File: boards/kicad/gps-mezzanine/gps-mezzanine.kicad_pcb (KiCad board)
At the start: 2 copper layers, 55 x 40 mm, 15 parts, among them P1 CONN_02X20, Q1 BSS138, Q2 BSS138, U1 MCP1700T-3302E/TT, U2 FGPMMOPA6H

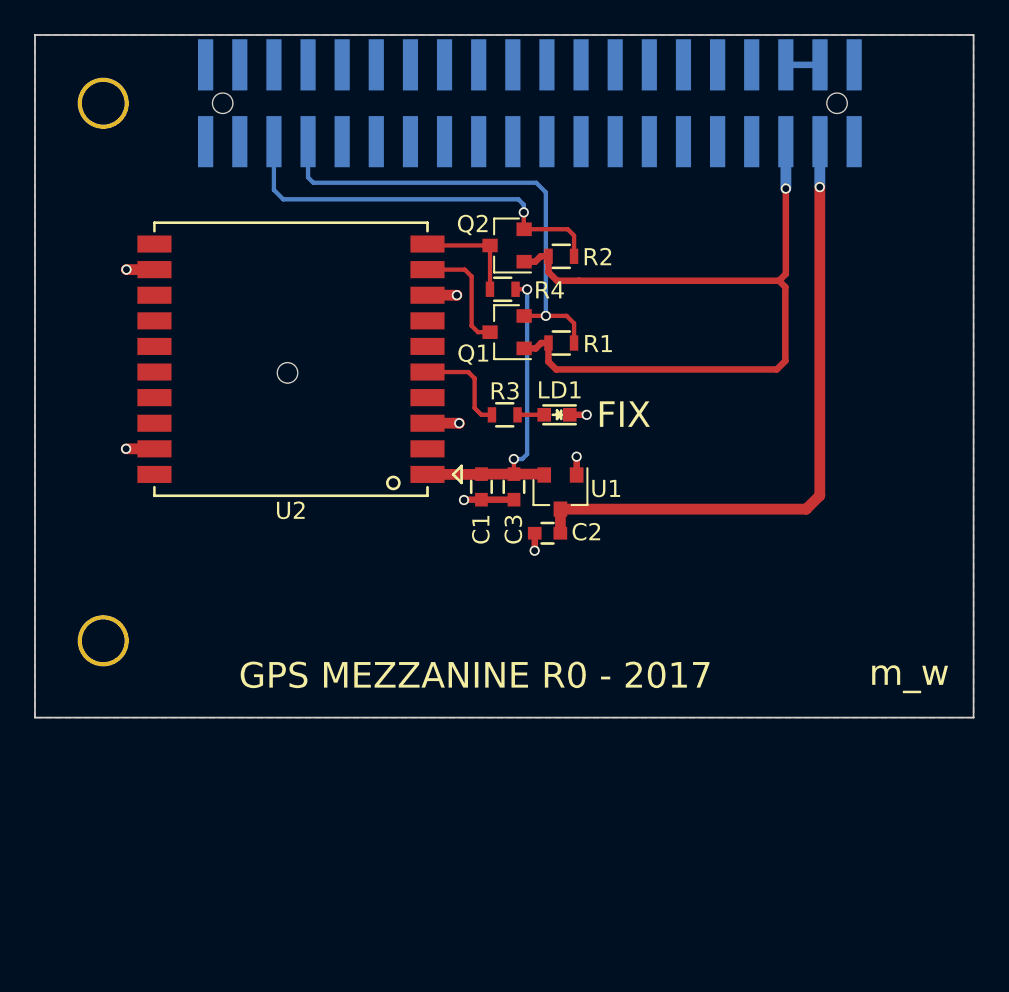
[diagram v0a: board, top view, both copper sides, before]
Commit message: Update GPS mezzanine
Adds CR2032 backup battery.
Adds uFL external antenna connector.
Connects PPS and fix signal to base board.
Switches to TXS0104 for level translation.

Signed-off-by: Michael Welling <mwelling@ieee.org>
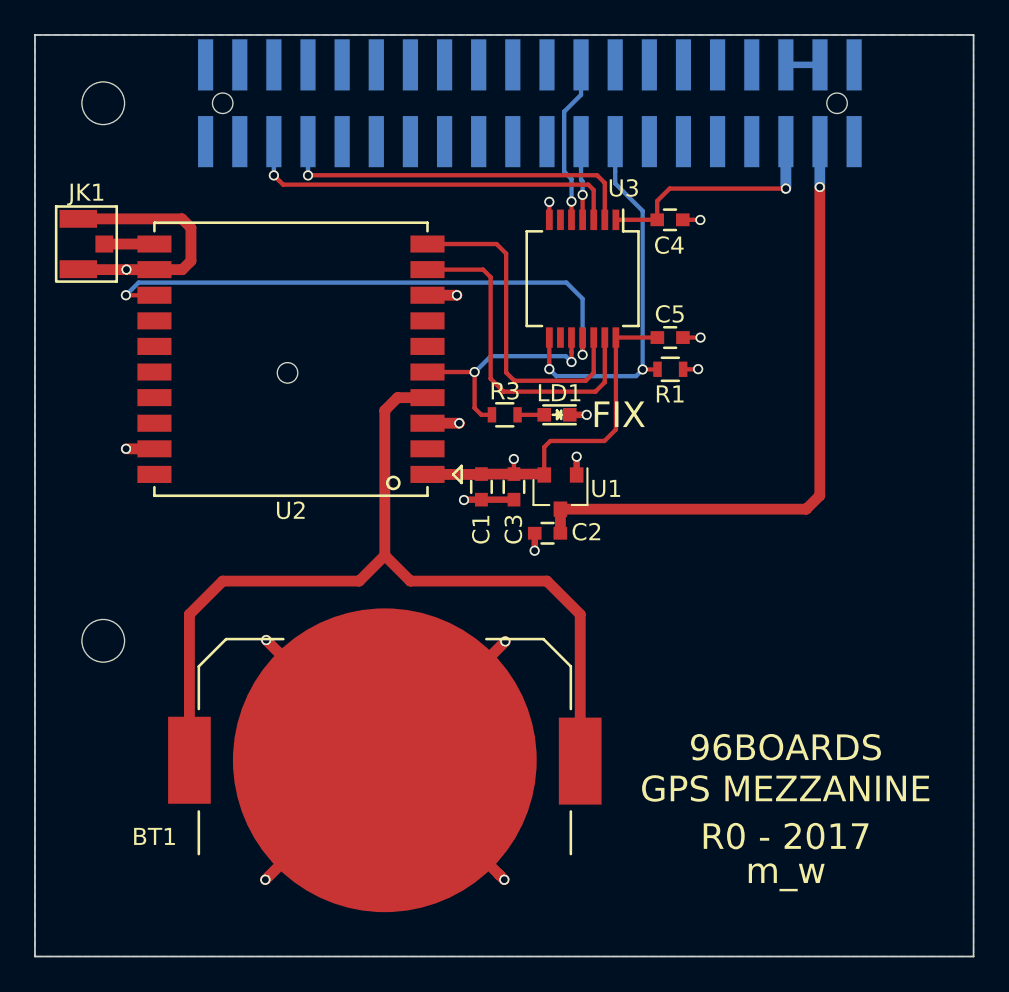
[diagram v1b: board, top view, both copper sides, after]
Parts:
- removed Q1, Q2: BSS138, TO_SOT_Packages_SMD:SOT-23
- removed R2, R4: 10K, Resistors_SMD:R_0603
- removed REF** (x2): Hole_2.5MM, Sensors:Hole_2.5MM
- added BT1: Battery_Cell, 96boards:BAT-HLD-001, F.Cu at (120.5, 142.5)
- added C4: .1uF, Capacitors_SMD:C_0603, F.Cu at (137.2, 110.8)
- added C5: .1uF, Capacitors_SMD:C_0603, F.Cu at (137.2, 117.7)
- added JK1: uFL, 96boards:U.FL-R-SMT-1, F.Cu at (102.5, 112.2)
- added MH1: M2.5, Mounting_Holes:MountingHole_2-5mm, F.Cu at (104.0, 104.0)
- added MH3: M2.5, Mounting_Holes:MountingHole_2-5mm, F.Cu at (104.0, 135.5)
- added U3: TXS0104E, Housings_SSOP:SSOP-14_5.3x6.2mm_Pitch0.65mm, F.Cu at (132.1, 114.3)
- R1: value 10K -> 1K
- moved R1 6.57 mm to (137.2, 119.6)
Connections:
- R1 pad 1: UART0_RX -> GND
- R1 pad 2: +1V8 -> GPIO_C
- U2 pad 13: Net-(U2-Pad13) -> GPS_1PPS
- U2 pad 4: Net-(U2-Pad4) -> +BATT
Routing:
- net GND: track 12.9 -> 70.5 mm, vias 8 -> 16
- net +BATT: track 0.00 -> 54.2 mm
- net GPS_1PPS: track 0.00 -> 33.4 mm, vias 0 -> 2
- net +1V8: track 46.3 -> 14.1 mm
- net GPIO_C: track 0.00 -> 22.5 mm, vias 0 -> 2
- net GPS_RX: track 6.27 -> 19.5 mm
- net GPS_TX: track 6.88 -> 19.7 mm
- net GPIO_B: track 0.00 -> 9.67 mm, vias 0 -> 1
- net FIX: track 5.83 -> 13.7 mm, vias 0 -> 2
- net UART0_RX: track 27.9 -> 21.7 mm
- net GPIO_A: track 0.00 -> 4.62 mm, vias 0 -> 1
- net Net-(JK1-Pad1): track 0.00 -> 2.94 mm
- net +3V3: track 19.0 -> 21.8 mm, vias 2 -> 1
- net UART0_TX: track 23.6 -> 22.8 mm
- removed copper zone on F.Cu, net GND
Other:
- board size 55 x 40 mm -> 55 x 54 mm
- board text added: "96BOARDS GPS MEZZANINE"
- board text added: "R0 - 2017"
- board text removed: "GPS MEZZANINE R0 - 2017"

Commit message: Add UART header and schematic PDF
Signed-off-by: Michael Welling <mwelling@ieee.org>
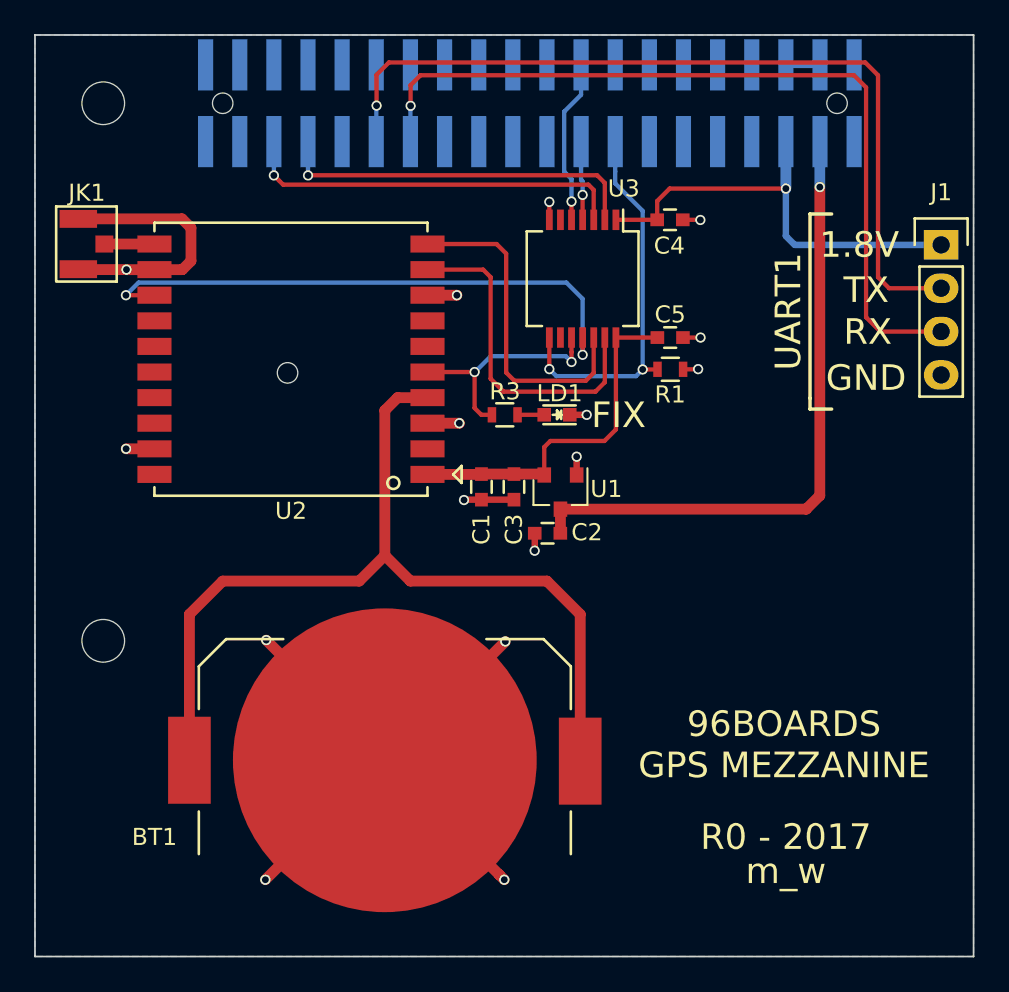
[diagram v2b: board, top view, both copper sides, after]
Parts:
- added J1: CONN_01X04, Pin_Headers:Pin_Header_Straight_1x04, F.Cu at (153.1, 112.3)
- renumbered MH3 to MH2
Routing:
- net UART1_TX: track 0.00 -> 49.7 mm, vias 0 -> 1
- net UART1_RX: track 0.00 -> 48.8 mm, vias 0 -> 1
- net +1V8: track 14.1 -> 26.2 mm
- net +3V3: track 21.8 -> 21.0 mm, vias 1 -> 0
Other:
- board text added: "1.8V"
- board text added: "GND"
- board text added: "RX"
- board text added: "TX"
- board text added: "UART1"
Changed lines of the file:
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@@
   (general
     (thickness 1.6)
-    (drawings 14)
-    (tracks 166)
+    (drawings 23)
+    (tracks 186)
     (zones 0)
-    (modules 16)
+    (modules 17)
     (nets 56)
   )
@@
     (add_net GND)
   )
+  (module Pin_Headers:Pin_Header_Straight_1x04 (layer F.Cu)
+    (at 153.1 112.3)
+    (descr "Through hole pin header")
+    (tags "pin header")
+    (fp_text reference J1 (at 0 -3.08) (layer F.SilkS)
+      (effects (font (size 1 1) (thickness 0.15)))
+    )
+    (fp_text value CONN_01X04 (at -0.7 -3.08) (layer F.Fab) hide
+      (effects (font (size 1 1) (thickness 0.15)))
+    )
+    (fp_line (start -1.75 -1.75) (end -1.75 9.4) (layer F.CrtYd) (width 0.05))
+    (fp_line (start 1.75 -1.75) (end 1.75 9.4) (layer F.CrtYd) (width 0.05))
+    (fp_line (start -1.75 -1.75) (end 1.75 -1.75) (layer F.CrtYd) (width 0.05))
+    (fp_line (start -1.75 9.4) (end 1.75 9.4) (layer F.CrtYd) (width 0.05))
+    (fp_line (start -1.27 1.27) (end -1.27 8.89) (layer F.SilkS) (width 0.15))
+    (fp_line (start 1.27 1.27) (end 1.27 8.89) (layer F.SilkS) (width 0.15))
+    (fp_line (start 1.55 -1.55) (end 1.55 0) (layer F.SilkS) (width 0.15))
+    (fp_line (start -1.27 8.89) (end 1.27 8.89) (layer F.SilkS) (width 0.15))
+    (fp_line (start 1.27 1.27) (end -1.27 1.27) (layer F.SilkS) (width 0.15))
+    (fp_line (start -1.55 0) (end -1.55 -1.55) (layer F.SilkS) (width 0.15))
+    (fp_line (start -1.55 -1.55) (end 1.55 -1.55) (layer F.SilkS) (width 0.15))
+    (pad 1 thru_hole rect (at 0 0) (size 2.032 1.7272) (drill 1.016) (layers *.Cu *.Mask F.SilkS)
+      (net 1 +1V8))
+    (pad 2 thru_hole oval (at 0 2.54) (size 2.032 1.7272) (drill 1.016) (layers *.Cu *.Mask F.SilkS)
+      (net 26 UART1_TX))
+    (pad 3 thru_hole oval (at 0 5.08) (size 2.032 1.7272) (drill 1.016) (layers *.Cu *.Mask F.SilkS)
+      (net 27 UART1_RX))
+    (pad 4 thru_hole oval (at 0 7.62) (size 2.032 1.7272) (drill 1.016) (layers *.Cu *.Mask F.SilkS)
+      (net 2 GND))
+    (model Pin_Headers.3dshapes/Pin_Header_Straight_1x04.wrl
+      (at (xyz 0 -0.15 0))
+      (scale (xyz 1 1 1))
+      (rotate (xyz 0 0 90))
+    )
+  )
   (module 96boards:U.FL-R-SMT-1 (layer F.Cu)
     (at 102.54 112.25 90)
@@
     (descr "Mounting hole, Befestigungsbohrung, 2,5mm, No Annular, Kein Restring,")
     (tags "Mounting hole, Befestigungsbohrung, 2,5mm, No Annular, Kein Restring,")
-    (fp_text reference MH3 (at 0 -3.50012) (layer F.SilkS) hide
+    (fp_text reference MH2 (at 0 -3.50012) (layer F.SilkS) hide
       (effects (font (size 1 1) (thickness 0.15)))
     )
@@
     )
   )
+  (gr_line (start 145.415 121.92) (end 146.685 121.92) (layer F.SilkS) (width 0.2))
+  (gr_line (start 145.415 121.285) (end 145.415 121.92) (layer F.SilkS) (width 0.2))
+  (gr_line (start 145.415 110.49) (end 145.415 121.285) (layer F.SilkS) (width 0.2))
+  (gr_line (start 146.685 110.49) (end 145.415 110.49) (layer F.SilkS) (width 0.2))
+  (gr_text UART1 (at 144.145 116.205 90) (layer F.SilkS)
+    (effects (font (size 1.5 1.5) (thickness 0.3)))
+  )
+  (gr_text GND (at 148.7 120.1) (layer F.SilkS)
+    (effects (font (size 1.5 1.5) (thickness 0.3)))
+  )
+  (gr_text RX (at 148.8 117.4) (layer F.SilkS)
+    (effects (font (size 1.5 1.5) (thickness 0.3)))
+  )
+  (gr_text TX (at 148.71 114.95) (layer F.SilkS)
+    (effects (font (size 1.5 1.5) (thickness 0.3)))
+  )
+  (gr_text 1.8V (at 148.3 112.3) (layer F.SilkS)
+    (effects (font (size 1.5 1.5) (thickness 0.3)))
+  )
   (gr_text m_w (at 144 149) (layer F.SilkS)
     (effects (font (size 1.5 1.5) (thickness 0.3)))
   )
-  (gr_text "96BOARDS\nGPS MEZZANINE" (at 144 143) (layer F.SilkS)
+  (gr_text "96BOARDS\nGPS MEZZANINE" (at 143.89 141.59) (layer F.SilkS)
     (effects (font (size 1.5 1.5) (thickness 0.3)))
   )
@@
   (gr_line (start 100 154) (end 100 100) (angle 90) (layer Edge.Cuts) (width 0.1))
   (gr_line (start 100 100) (end 155 100) (angle 90) (layer Edge.Cuts) (width 0.1))
+  (segment (start 144.52 112.3) (end 153.1 112.3) (width 0.381) (layer B.Cu) (net 1))
+  (segment (start 144 111.78) (end 144.52 112.3) (width 0.381) (layer B.Cu) (net 1))
+  (segment (start 144 109) (end 144 111.78) (width 0.381) (layer B.Cu) (net 1))
   (segment (start 136.46 110.83) (end 134.04 110.83) (width 0.254) (layer F.Cu) (net 1))
   (segment (start 137.19 109) (end 136.46 109.73) (width 0.254) (layer F.Cu) (net 1))
@@
   (via (at 144 109) (size 0.6) (drill 0.4) (layers F.Cu B.Cu) (net 1))
   (segment (start 120.55 142.46) (end 113.55 135.46) (width 0.635) (layer F.Cu) (net 2))
-  (via (at 113.55 135.46) (size 0.6) (drill 0.4) (layers F.Cu B.Cu) (net 2) (status 1000000))
+  (via (at 113.55 135.46) (size 0.6) (drill 0.4) (layers F.Cu B.Cu) (net 2))
   (segment (start 120.56 142.54) (end 127.56 135.54) (width 0.635) (layer F.Cu) (net 2))
   (via (at 127.56 135.54) (size 0.6) (drill 0.4) (layers F.Cu B.Cu) (net 2))
@@
   (segment (start 132.09 110.83) (end 132.09 109.37) (width 0.254) (layer F.Cu) (net 12))
   (via (at 132.09 109.37) (size 0.6) (drill 0.4) (layers F.Cu B.Cu) (net 12))
+  (segment (start 120.015 104.14) (end 120.015 102.335) (width 0.254) (layer F.Cu) (net 26))
+  (segment (start 120.015 102.335) (end 120.74 101.61) (width 0.254) (layer F.Cu) (net 26))
+  (segment (start 120.74 101.61) (end 148.65 101.61) (width 0.254) (layer F.Cu) (net 26))
+  (segment (start 148.65 101.61) (end 149.4 102.36) (width 0.254) (layer F.Cu) (net 26))
+  (segment (start 149.4 102.36) (end 149.4 114.19) (width 0.254) (layer F.Cu) (net 26))
+  (segment (start 149.4 114.19) (end 150.05 114.84) (width 0.254) (layer F.Cu) (net 26))
+  (segment (start 150.05 114.84) (end 153.1 114.84) (width 0.254) (layer F.Cu) (net 26))
+  (segment (start 120 106.25) (end 120 104.155) (width 0.254) (layer B.Cu) (net 26))
+  (segment (start 120 104.155) (end 120.015 104.14) (width 0.254) (layer B.Cu) (net 26))
+  (via (at 120.015 104.14) (size 0.6) (drill 0.4) (layers F.Cu B.Cu) (net 26))
+  (segment (start 122.01 104.15) (end 122.01 102.94) (width 0.254) (layer F.Cu) (net 27))
+  (segment (start 122.01 102.94) (end 122.59 102.36) (width 0.254) (layer F.Cu) (net 27))
+  (segment (start 122.59 102.36) (end 147.99 102.36) (width 0.254) (layer F.Cu) (net 27))
+  (segment (start 147.99 102.36) (end 148.7 103.07) (width 0.254) (layer F.Cu) (net 27))
+  (segment (start 148.7 116.54) (end 149.54 117.38) (width 0.254) (layer F.Cu) (net 27))
+  (segment (start 149.54 117.38) (end 153.1 117.38) (width 0.254) (layer F.Cu) (net 27))
+  (segment (start 148.7 103.07) (end 148.7 116.54) (width 0.254) (layer F.Cu) (net 27))
+  (segment (start 122 106.25) (end 122 104.16) (width 0.254) (layer B.Cu) (net 27))
+  (segment (start 122 104.16) (end 122.01 104.15) (width 0.254) (layer B.Cu) (net 27))
+  (via (at 122.01 104.15) (size 0.6) (drill 0.4) (layers F.Cu B.Cu) (net 27))
   (segment (start 135.61 119.6) (end 135.22 119.99) (width 0.254) (layer B.Cu) (net 28))
   (segment (start 135.22 119.99) (end 130.55 119.99) (width 0.254) (layer B.Cu) (net 28))
@@
   (segment (start 129.840995 125.785215) (end 129.840995 124.149005) (width 0.254) (layer F.Cu) (net 39))
   (segment (start 136.47 117.73) (end 134.04 117.73) (width 0.254) (layer F.Cu) (net 39))
-  (segment (start 128.067 125.73) (end 128.067 124.857) (width 0.254) (layer F.Cu) (net 39))
-  (segment (start 128.067 124.857) (end 128.06 124.85) (width 0.254) (layer F.Cu) (net 39))
-  (via (at 128.06 124.85) (size 0.6) (drill 0.4) (layers F.Cu B.Cu) (net 39))
   (segment (start 128.067 125.73) (end 129.78578 125.73) (width 0.635) (layer F.Cu) (net 39))
   (segment (start 129.78578 125.73) (end 129.840995 125.785215) (width 0.635) (layer F.Cu) (net 39))
